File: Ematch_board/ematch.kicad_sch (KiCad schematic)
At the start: 56 parts, among them J1 Conn_01x02_Male, J2 Conn_01x02_Male, J3 Conn_01x02_Male, J4 Conn_01x02_Male, J5 Conn_01x02_Male, J6 Conn_01x02_Male, Q51 PMV20ENR, Q52 PMV20ENR, Q53 PMV20ENR, Q54 PMV20ENR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

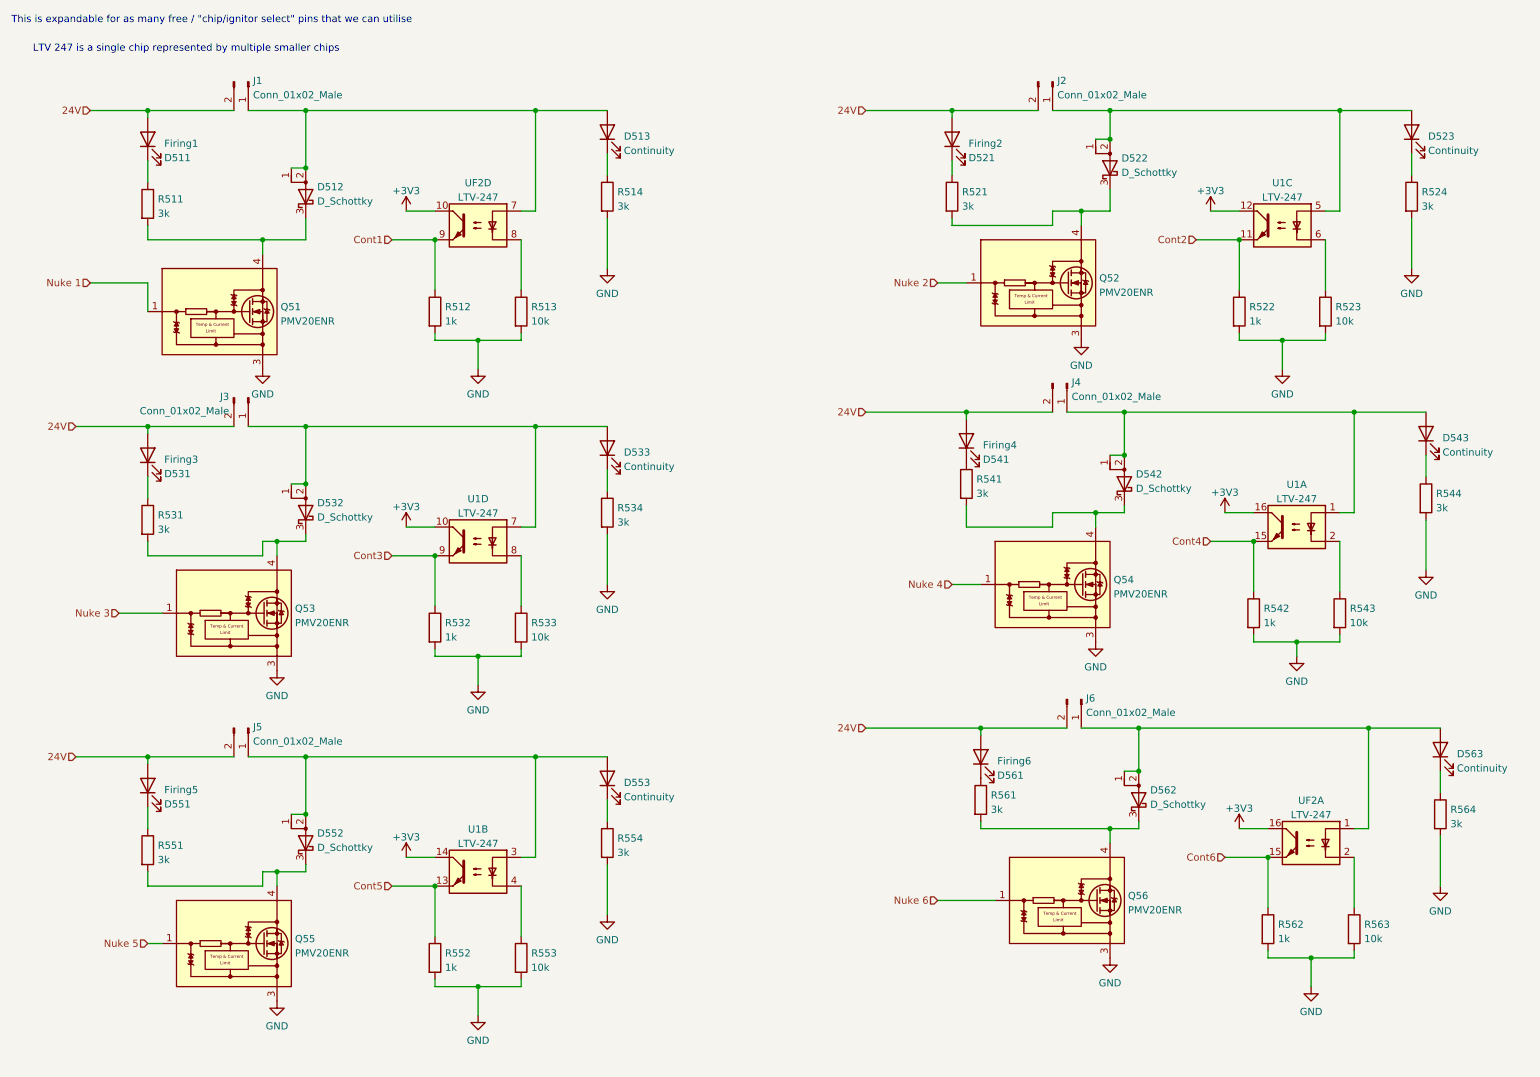
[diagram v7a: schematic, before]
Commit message: updated leds on ematch board and re-routed
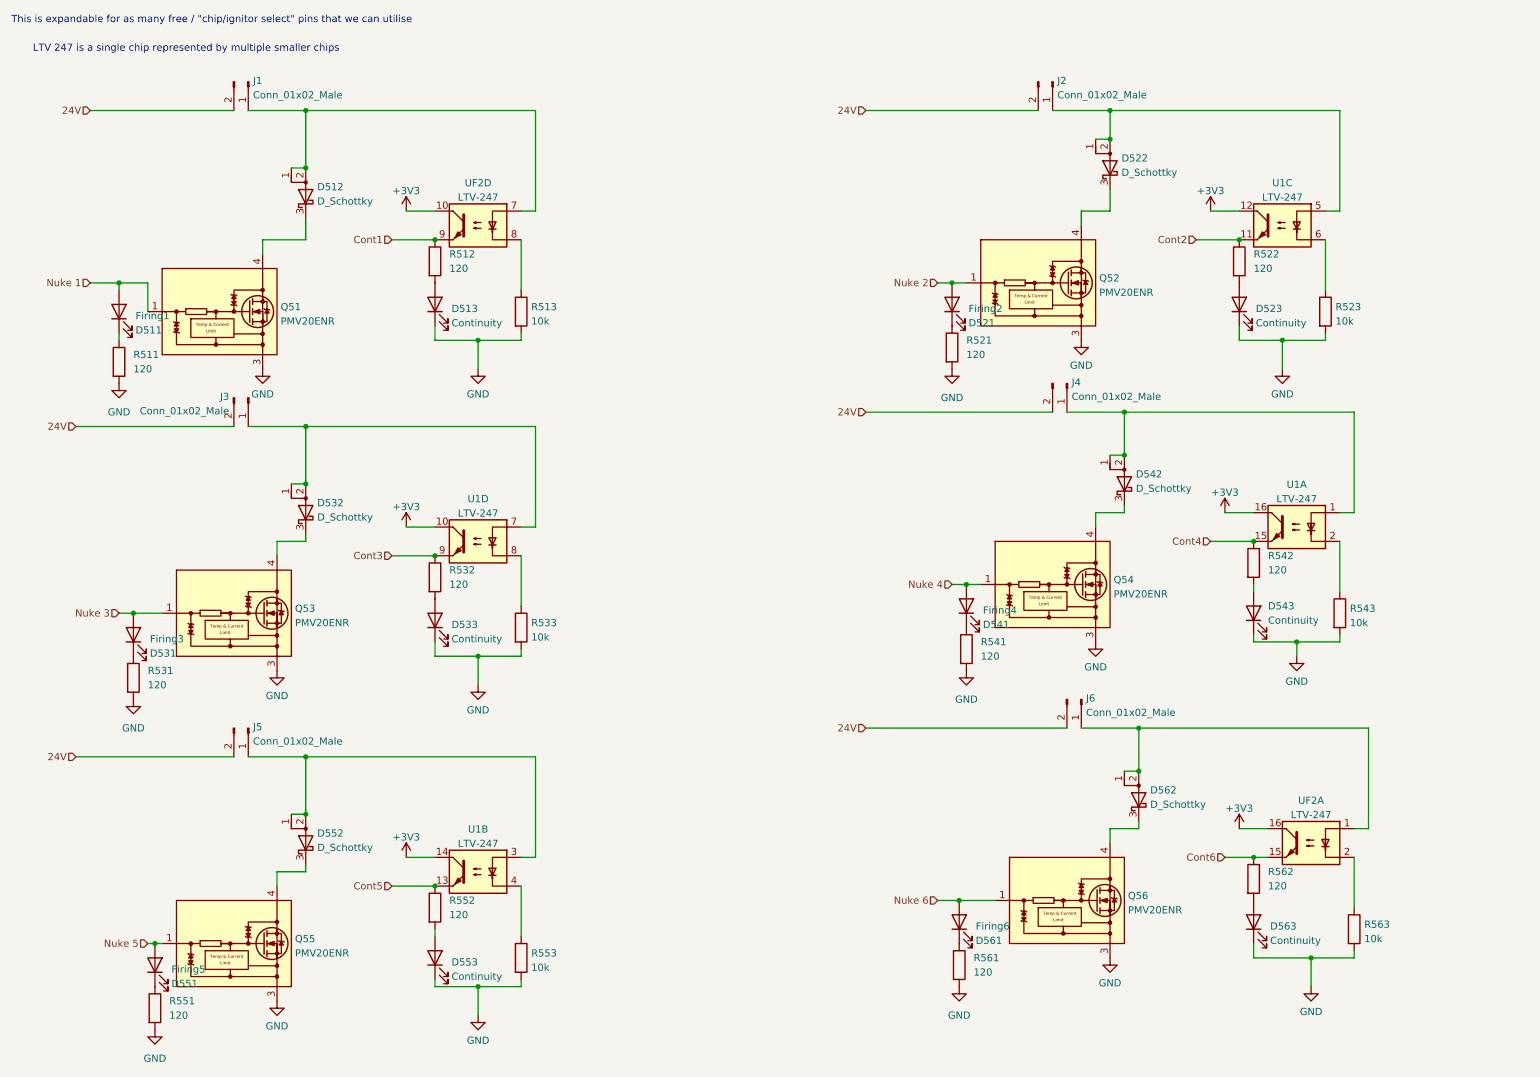
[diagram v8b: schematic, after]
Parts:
- removed R514, R524, R534, R544, R554, R564: 3k, Resistor_SMD:R_0603_1608Metric, symbol Device:R
- R511, R521, R531, R541, R551, R561: value 3k -> 120
- R512, R522, R532, R542, R552, R562: value 1k -> 120
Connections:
- net 24V: no longer Firing1.2 (A), Firing2.2 (A), Firing3.2 (A), Firing4.2 (A), Firing5.2 (A), Firing6.2 (A)
- net GND: now also D513.1 (K), D523.1 (K), D533.1 (K), D543.1 (K), D553.1 (K), D563.1 (K), R511.2, R521.2, R531.2, R541.2, R551.2, R561.2; no longer R512.2, R522.2, R532.2, R542.2, R552.2, R562.2
- net Nuke 1: now also Firing1.2 (A)
- net Nuke 2: now also Firing2.2 (A)
- net Nuke 3: now also Firing3.2 (A)
- net Nuke 4: now also Firing4.2 (A)
- net Nuke 5: now also Firing5.2 (A)
- net Nuke 6: now also Firing6.2 (A)
- net at D512.1 (A), D512.2 (A), J1.1 (Pin_1)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: no longer D513.2 (A)
- net at D512.3 (K), Q51.2 (D), Q51.4 (D): no longer R511.2
- net at D542.1 (A), D542.2 (A), J4.1 (Pin_1)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: no longer D543.2 (A)
- net at D552.1 (A), D552.2 (A), J5.1 (Pin_1)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: no longer D553.2 (A)
- net at D532.1 (A), D532.2 (A), J3.1 (Pin_1)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: no longer D533.2 (A)
- net at D522.1 (A), D522.2 (A), J2.1 (Pin_1)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: no longer D523.2 (A)
- net at D522.3 (K), Q52.2 (D), Q52.4 (D): no longer R521.2
- net at D552.3 (K), Q55.2 (D), Q55.4 (D): no longer R551.2
- net at D562.1 (A), D562.2 (A), J6.1 (Pin_1)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: no longer D563.2 (A)
- net at D532.3 (K), Q53.2 (D), Q53.4 (D): no longer R531.2
- net at D562.3 (K), Q56.2 (D), Q56.4 (D): no longer R561.2
- net at D542.3 (K), Q54.2 (D), Q54.4 (D): no longer R541.2
- new net: D543.2 (A), R542.2
- new net: D553.2 (A), R552.2
- new net: D563.2 (A), R562.2
- new net: D523.2 (A), R522.2
- new net: D533.2 (A), R532.2
- new net: D513.2 (A), R512.2
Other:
- moved on the sheet: D513, D523, D533, D543, D553, D563, Firing1, Firing2, Firing3, Firing4, Firing5, Firing6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
